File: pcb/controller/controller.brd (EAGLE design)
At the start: 73.7 x 76.2 mm, 101 parts, among them J1 SNG-2MM-HEADER-04-V, J2 DL-1.25MM-HEADER-20, J3 MICRO_SD, J4 SNG-100-HEADER-01-HDR-V, J5 7498011122R, J6 USB_A, J7 DL-1.25MM-HEADER-10, J8 CUI-PJ-013C, J9 SNG-100-HEADER-05-HDR-V, Q1 12MHz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

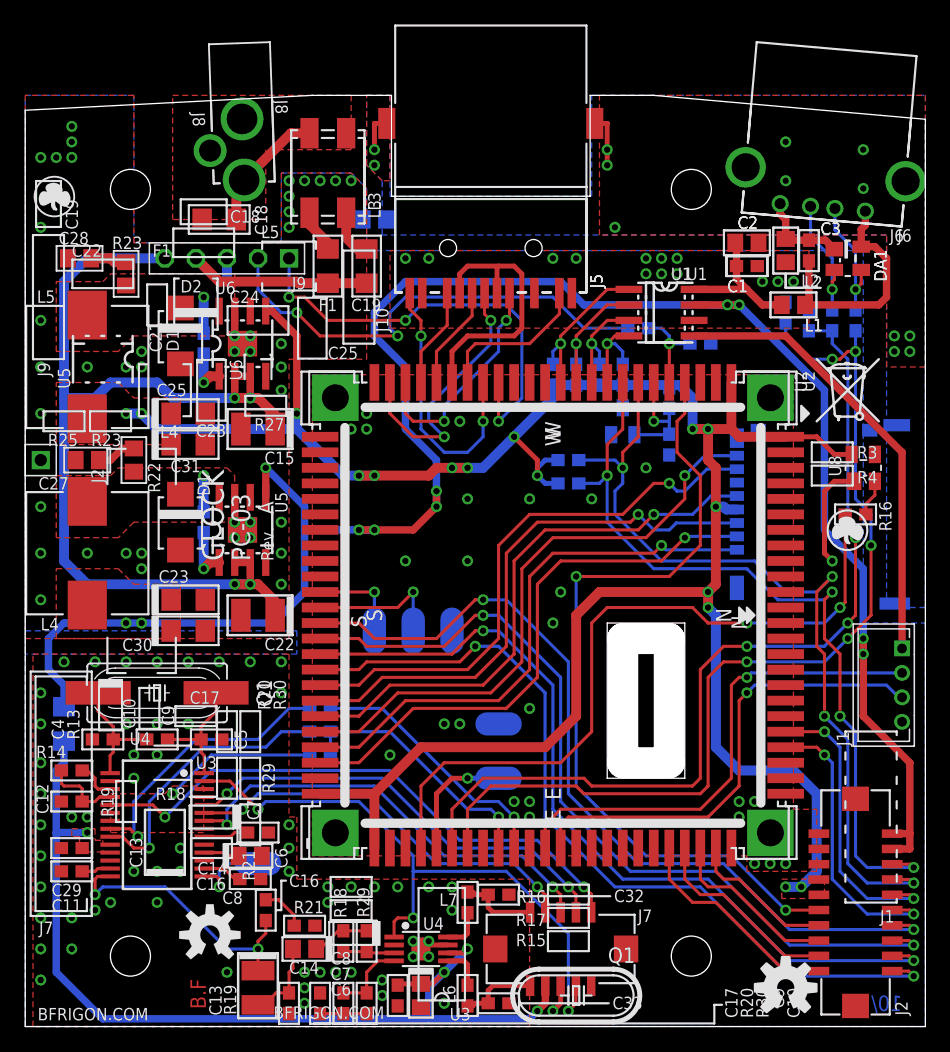
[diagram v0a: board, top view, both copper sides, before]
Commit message: Added a temperature sensor IC (U9) to controller PCB
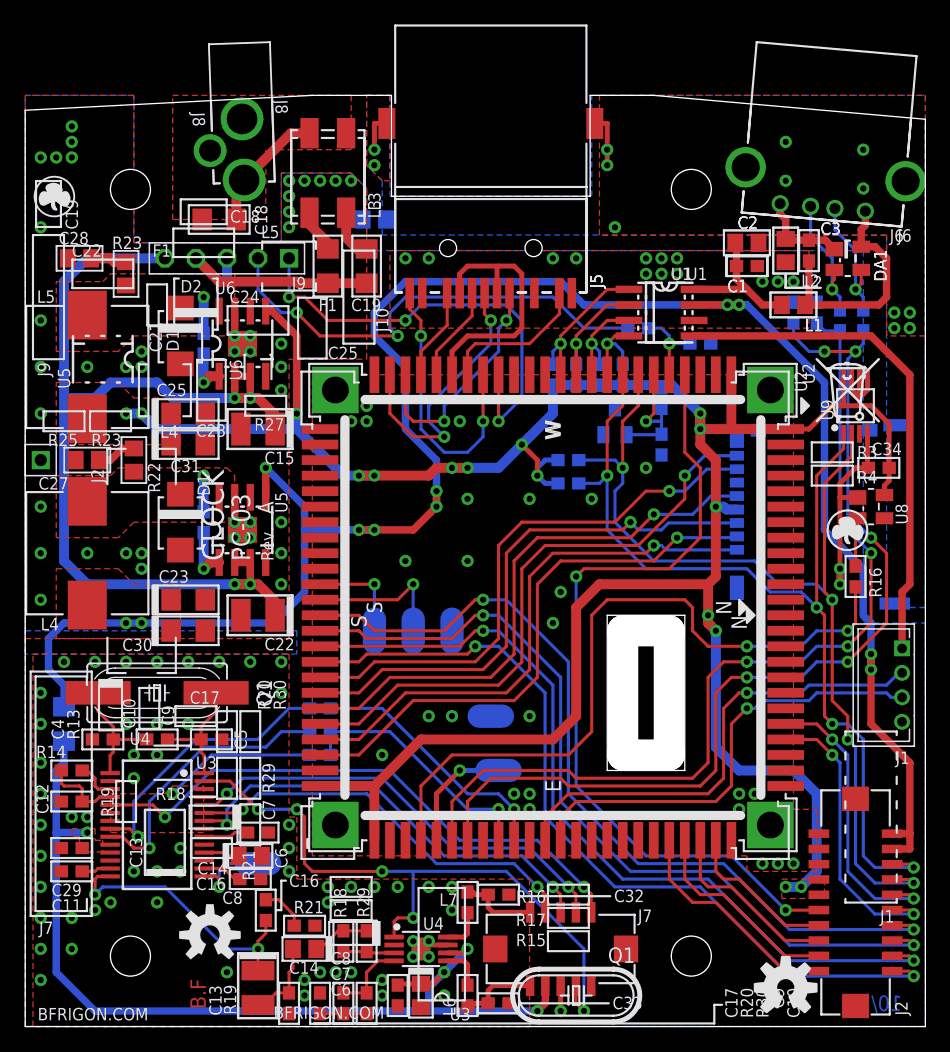
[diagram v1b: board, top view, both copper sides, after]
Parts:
- added C34: 100nF, Passive:SMD_0603
- added U9: MCP9804-E/MS, IC:MSOP8
- moved R16 5.08 mm to (67.9, 36.8), turned to 270 degrees
- moved U8 3.24 mm to (69.2, 42.5), turned to 270 degrees
- moved TP2 0.90 mm to (38.1, 25.4)
- moved R12 0.90 mm to (64.8, 58.4)
- moved R11 0.64 mm to (62.9, 58.4)
- moved R9 0.64 mm to (68.6, 57.8)
- moved U7 0.64 mm to (48.3, 49.5)
- moved C26 0.63 mm to (52.1, 47.6)
- moved R28 0.63 mm to (52.1, 51.4)
- moved TP1 0.63 mm to (38.7, 21.0)
- moved U2 0.63 mm to (43.2, 34.3)
- moved R10 0.63 mm to (66.7, 57.8)
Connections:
- net VCC renamed V_IN
- net 3.3V: now also C34.2, U9.5, U9.6, U9.7, U9.8
- net GND: now also C34.1, U9.4
- net SCL0: now also U9.2
- net SDA0: now also U9.1
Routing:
- net 3.3V: track 193.4 -> 212.3 mm
- net SDA0: track 65.8 -> 79.7 mm
- net SCL0: track 69.4 -> 81.6 mm
- net GND: track 23.1 -> 29.4 mm
- net USBB_5V: track 37.0 -> 41.6 mm
- net USBC_D+: track 39.1 -> 37.2 mm
- net DAC_SHDN: track 51.7 -> 53.2 mm, vias 3 -> 5
- net USBC_D-: track 40.7 -> 39.3 mm
- net 5V_AUD: track 78.4 -> 77.2 mm
- net NRST: track 59.5 -> 58.3 mm
- net N$21: track 3.01 -> 4.09 mm
- net USBA_D+: track 74.5 -> 75.3 mm
- net SD_DAT0: track 46.4 -> 45.6 mm
- net SD_CMD: track 45.6 -> 44.9 mm
- net VREF: track 9.67 -> 10.4 mm
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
